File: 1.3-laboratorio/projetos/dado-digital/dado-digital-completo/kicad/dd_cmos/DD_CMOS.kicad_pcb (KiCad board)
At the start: 2 copper layers, 50.8 x 38.1 mm, 11 parts, among them J1 Conn_01x02, J2 Conn_01x02, J4 Conn_01x01, J5 Conn_01x02, Q1 BC547

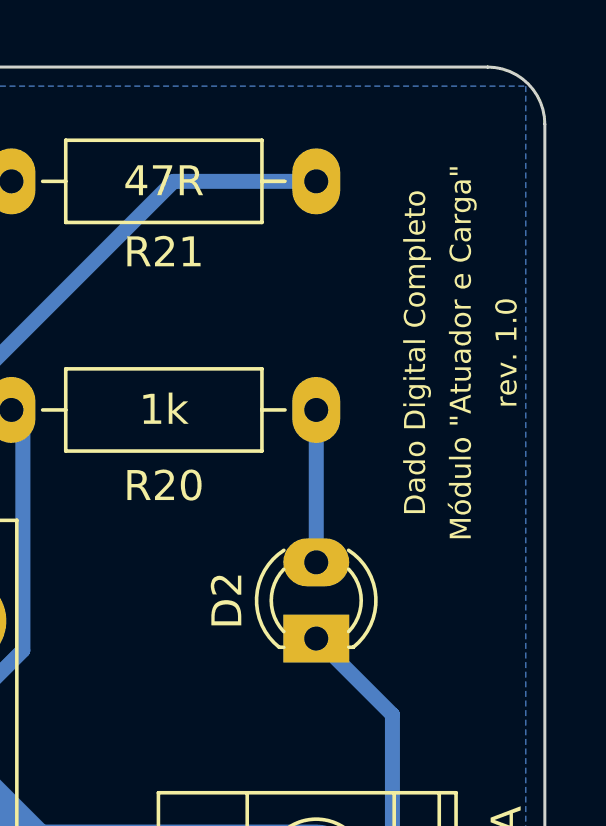
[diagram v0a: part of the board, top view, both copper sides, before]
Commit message: Roteiro do projeto semestral atualizado, incluindo acréscimo de datasheets e detalhes de montagem da PCI do bloco 'Atuador e Carga'.
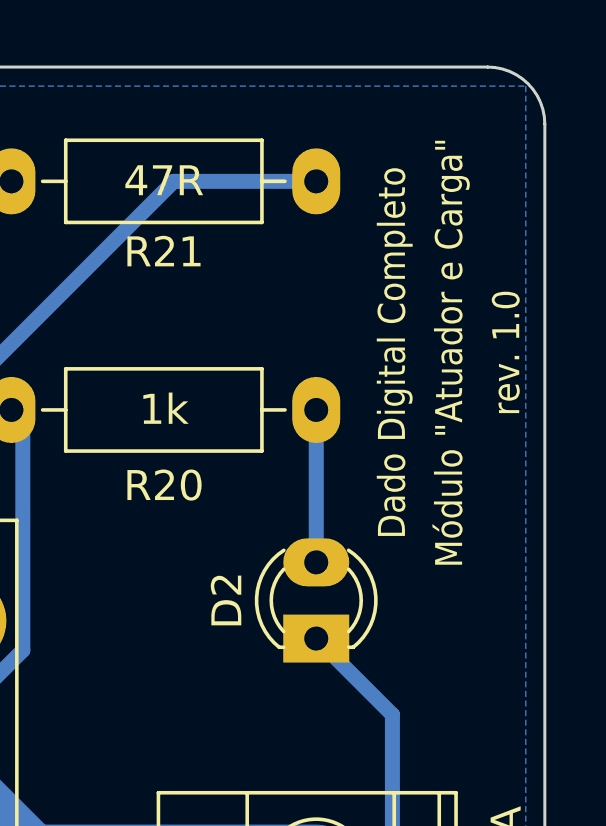
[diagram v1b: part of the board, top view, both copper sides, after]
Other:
- board text added: "Numeração da Revisão: a.b.c a: revisão principal, igual à revisão do esquema elétrico; se houver alteração elétrica, este número será alterado. b: revisão secundária, indicando alteração de leiaute; por exemplo, posicionamento de componentes, dimensões da placa, trilhas, ilhas. c: revisão menor, indicando apenas alguns ajustes gráficos, mas sem qualquer alteração de leiaute; por exemplo, reposici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"

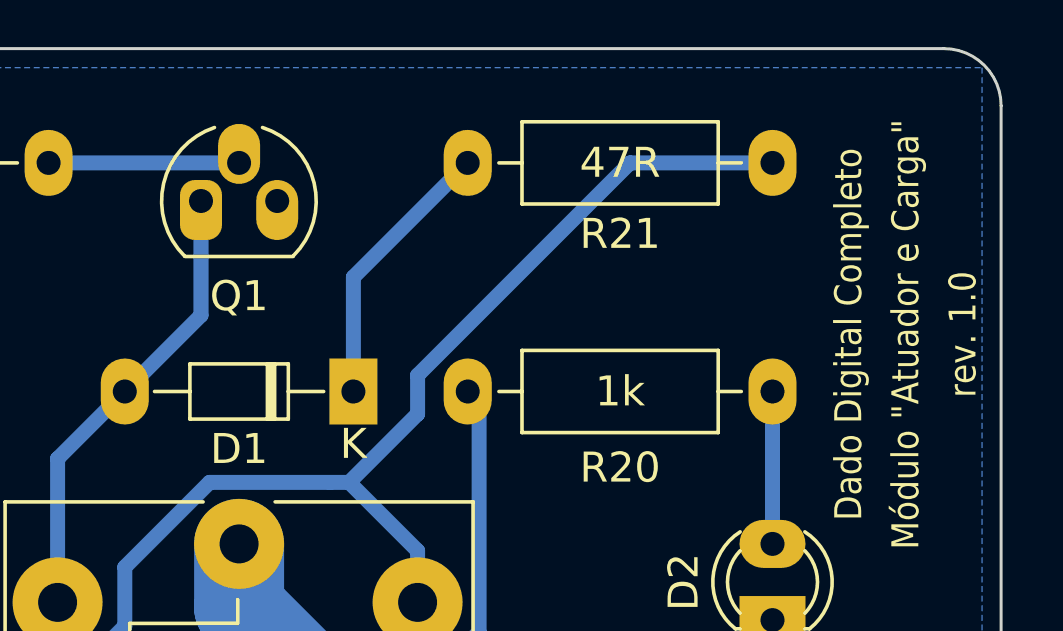
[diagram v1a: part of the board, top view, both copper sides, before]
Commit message: Datasheets, atualização de biblioteca do KiCad, P2 e P1/2022 de ETE102/N, detalhes em projetos.
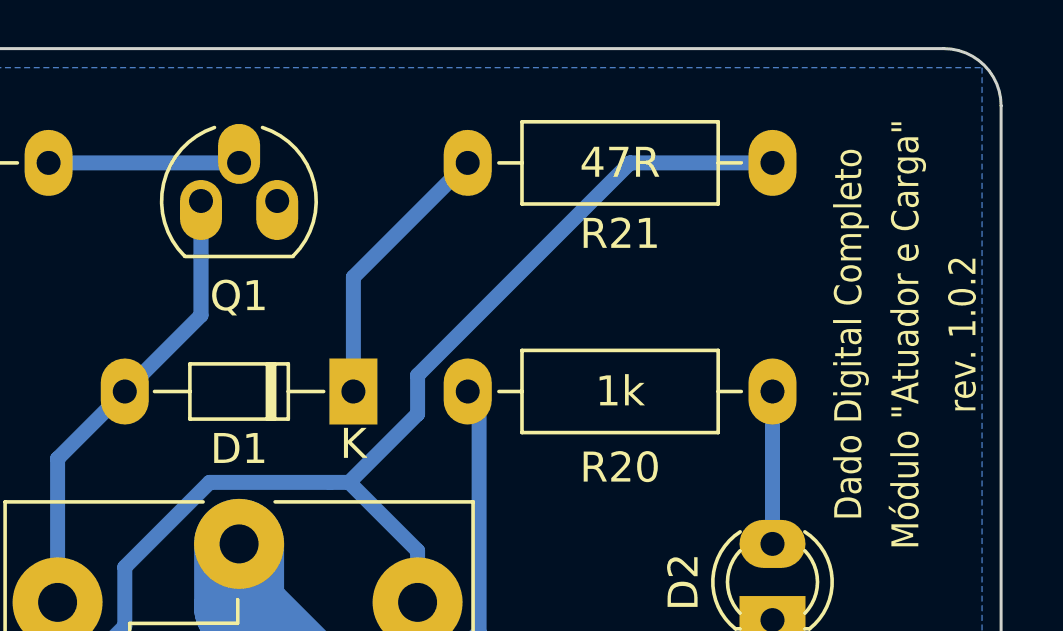
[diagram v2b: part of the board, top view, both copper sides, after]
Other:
- board text added: "Numeração da Revisão: a.b.c a: revisão principal, igual à revisão do esquema elétrico; se houver alteração elétrica, este número será alterado. b: revisão secundária, indicando alteração de leiaute; por exemplo, posicionamento de componentes, dimensões da placa, trilhas, ilhas. c: revisão menor, indicando apenas alguns ajustes gráficos, mas sem qualquer alteração de leiaute ou alguma alteração de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"
- board text added: "rev. 1.0.2"
- board text removed: "Numeração da Revisão: a.b.c a: revisão principal, igual à revisão do esquema elétrico; se houver alteração elétrica, este número será alterado. b: revisão secundária, indicando alteração de leiaute; por exemplo, posicionamento de componentes, dimensões da placa, trilhas, ilhas. c: revisão menor, indicando apenas alguns ajustes gráficos, mas sem qualquer alteração de leiaute; por exemplo, reposici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"
- board text removed: "rev. 1.0"
